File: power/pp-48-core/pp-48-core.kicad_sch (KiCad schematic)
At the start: 0 parts

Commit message: pp-48 chained plane: unit board 76 x 72 (9 mm left margin for chain IN J301 + holes, user; slots as rev1 at x 100 / 125; 17 mm input strip with XT60, unit hot-swap, chain OUT J302) and core board 56 x 72 (rev1 core minus the tile, 8 mm right margin for chain OUT J301 + holes, mux U6 by the header, XT30 at the bottom) placed as drafts by tools/place_unit.py / place_core.py (boardfit.py helpers); chain headers on B, pins at v 39..61 on every board; pinout swapped so IN pin 1 = 3V3 / P0 at the bottom on B (flat cable n -> 13 - n); DRC 0 errors besides unconnected, parity clean; not routed; handoff
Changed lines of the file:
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@@
+			)
+		)
+		(pin "UNIT4_SCL" bidirectional
+			(at 127 193.04 180)
+			(effects
+				(font
+					(size 1.27 1.27)
+				)
+				(justify left)
+			)
+		)
+		(pin "UNIT4_SDA" bidirectional
+			(at 127 195.58 180)
+			(effects
+				(font
+					(size 1.27 1.27)
+				)
+				(justify left)
+			)
+		)
+		(pin "UNIT3_SCL" bidirectional
+			(at 127 198.12 180)
+			(effects
+				(font
+					(size 1.27 1.27)
+				)
+				(justify left)
+			)
+		)
+		(pin "UNIT3_SDA" bidirectional
+			(at 127 200.66 180)
+			(effects
+				(font
+					(size 1.27 1.27)
+				)
+				(justify left)
+			)
+		)
+		(pin "UNIT2_SCL" bidirectional
+			(at 127 203.2 180)
+			(effects
+				(font
+					(size 1.27 1.27)
+				)
+				(justify left)
+			)
+		)
+		(pin "UNIT2_SDA" bidirectional
+			(at 127 205.74 180)
+			(effects
+				(font
+					(size 1.27 1.27)
+				)
+				(justify left)
+			)
+		)
+		(pin "UNIT1_SCL" bidirectional
+			(at 127 208.28 180)
+			(effects
+				(font
+					(size 1.27 1.27)
+				)
+				(justify left)
 			)
 		)
 		(pin "UNIT1_SDA" bidirectional
-			(at 127 193.04 180)
-			(effects
-				(font
-					(size 1.27 1.27)
-				)
-				(justify left)
-			)
-		)
-		(pin "UNIT1_SCL" bidirectional
-			(at 127 195.58 180)
-			(effects
-				(font
-					(size 1.27 1.27)
-				)
-				(justify left)
-			)
-		)
-		(pin "UNIT2_SDA" bidirectional
-			(at 127 198.12 180)
-			(effects
-				(font
-					(size 1.27 1.27)
-				)
-				(justify left)
-			)
-		)
-		(pin "UNIT2_SCL" bidirectional
-			(at 127 200.66 180)
-			(effects
-				(font
-					(size 1.27 1.27)
-				)
-				(justify left)
-			)
-		)
-		(pin "UNIT3_SDA" bidirectional
-			(at 127 203.2 180)
-			(effects
-				(font
-					(size 1.27 1.27)
-				)
-				(justify left)
-			)
-		)
-		(pin "UNIT3_SCL" bidirectional
-			(at 127 205.74 180)
-			(effects
-				(font
-					(size 1.27 1.27)
-				)
-				(justify left)
-			)
-		)
-		(pin "UNIT4_SDA" bidirectional
-			(at 127 208.28 180)
-			(effects
-				(font
-					(size 1.27 1.27)
-				)
-				(justify left)
-			)
-		)
-		(pin "UNIT4_SCL" bidirectional
 			(at 127 210.82 180)
 			(effects
@@
 		)
 	)
+	(label "UNIT4_SCL"
+		(at 119.38 193.04 180)
+		(effects
+			(font
+				(size 1.27 1.27)
+			)
+			(justify right bottom)
+		)
+	)
+	(wire
+		(pts
+			(xy 127 195.58) (xy 119.38 195.58)
+		)
+		(stroke
+			(width 0)
+			(type default)
+		)
+	)
+	(label "UNIT4_SDA"
+		(at 119.38 195.58 180)
+		(effects
+			(font
+				(size 1.27 1.27)
+			)
+			(justify right bottom)
+		)
+	)
+	(wire
+		(pts
+			(xy 127 198.12) (xy 119.38 198.12)
+		)
+		(stroke
+			(width 0)
+			(type default)
+		)
+	)
+	(label "UNIT3_SCL"
+		(at 119.38 198.12 180)
+		(effects
+			(font
+				(size 1.27 1.27)
+			)
+			(justify right bottom)
+		)
+	)
+	(wire
+		(pts
+			(xy 127 200.66) (xy 119.38 200.66)
+		)
+		(stroke
+			(width 0)
+			(type default)
+		)
+	)
+	(label "UNIT3_SDA"
+		(at 119.38 200.66 180)
+		(effects
+			(font
+				(size 1.27 1.27)
+			)
+			(justify right bottom)
+		)
+	)
+	(wire
+		(pts
+			(xy 127 203.2) (xy 119.38 203.2)
+		)
+		(stroke
+			(width 0)
+			(type default)
+		)
+	)
+	(label "UNIT2_SCL"
+		(at 119.38 203.2 180)
+		(effects
+			(font
+				(size 1.27 1.27)
+			)
+			(justify right bottom)
+		)
+	)
+	(wire
+		(pts
+			(xy 127 205.74) (xy 119.38 205.74)
+		)
+		(stroke
+			(width 0)
+			(type default)
+		)
+	)
+	(label "UNIT2_SDA"
+		(at 119.38 205.74 180)
+		(effects
+			(font
+				(size 1.27 1.27)
+			)
+			(justify right bottom)
+		)
+	)
+	(wire
+		(pts
+			(xy 127 208.28) (xy 119.38 208.28)
+		)
+		(stroke
+			(width 0)
+			(type default)
+		)
+	)
+	(label "UNIT1_SCL"
+		(at 119.38 208.28 180)
+		(effects
+			(font
+				(size 1.27 1.27)
+			)
+			(justify right bottom)
+		)
+	)
+	(wire
+		(pts
+			(xy 127 210.82) (xy 119.38 210.82)
+		)
+		(stroke
+			(width 0)
+			(type default)
+		)
+	)
 	(label "UNIT1_SDA"
-		(at 119.38 193.04 180)
-		(effects
-			(font
-				(size 1.27 1.27)
-			)
-			(justify right bottom)
-		)
-	)
-	(wire
-		(pts
-			(xy 127 195.58) (xy 119.38 195.58)
-		)
-		(stroke
-			(width 0)
-			(type default)
-		)
-	)
-	(label "UNIT1_SCL"
-		(at 119.38 195.58 180)
-		(effects
-			(font
-				(size 1.27 1.27)
-			)
-			(justify right bottom)
-		)
-	)
-	(wire
-		(pts
-			(xy 127 198.12) (xy 119.38 198.12)
-		)
-		(stroke
-			(width 0)
-			(type default)
-		)
-	)
-	(label "UNIT2_SDA"
-		(at 119.38 198.12 180)
-		(effects
-			(font
-				(size 1.27 1.27)
-			)
-			(justify right bottom)
-		)
-	)
-	(wire
-		(pts
-			(xy 127 200.66) (xy 119.38 200.66)
-		)
-		(stroke
-			(width 0)
-			(type default)
-		)
-	)
-	(label "UNIT2_SCL"
-		(at 119.38 200.66 180)
-		(effects
-			(font
-				(size 1.27 1.27)
-			)
-			(justify right bottom)
-		)
-	)
-	(wire
-		(pts
-			(xy 127 203.2) (xy 119.38 203.2)
-		)
-		(stroke
-			(width 0)
-			(type default)
-		)
-	)
-	(label "UNIT3_SDA"
-		(at 119.38 203.2 180)
-		(effects
-			(font
-				(size 1.27 1.27)
-			)
-			(justify right bottom)
-		)
-	)
-	(wire
-		(pts
-			(xy 127 205.74) (xy 119.38 205.74)
-		)
-		(stroke
-			(width 0)
-			(type default)
-		)
-	)
-	(label "UNIT3_SCL"
-		(at 119.38 205.74 180)
-		(effects
-			(font
-				(size 1.27 1.27)
-			)
-			(justify right bottom)
-		)
-	)
-	(wire
-		(pts
-			(xy 127 208.28) (xy 119.38 208.28)
-		)
-		(stroke
-			(width 0)
-			(type default)
-		)
-	)
-	(label "UNIT4_SDA"
-		(at 119.38 208.28 180)
-		(effects
-			(font
-				(size 1.27 1.27)
-			)
-			(justify right bottom)
-		)
-	)
-	(wire
-		(pts
-			(xy 127 210.82) (xy 119.38 210.82)
-		)
-		(stroke
-			(width 0)
-			(type default)
-		)
-	)
-	(label "UNIT4_SCL"
 		(at 119.38 210.82 180)
 		(effects

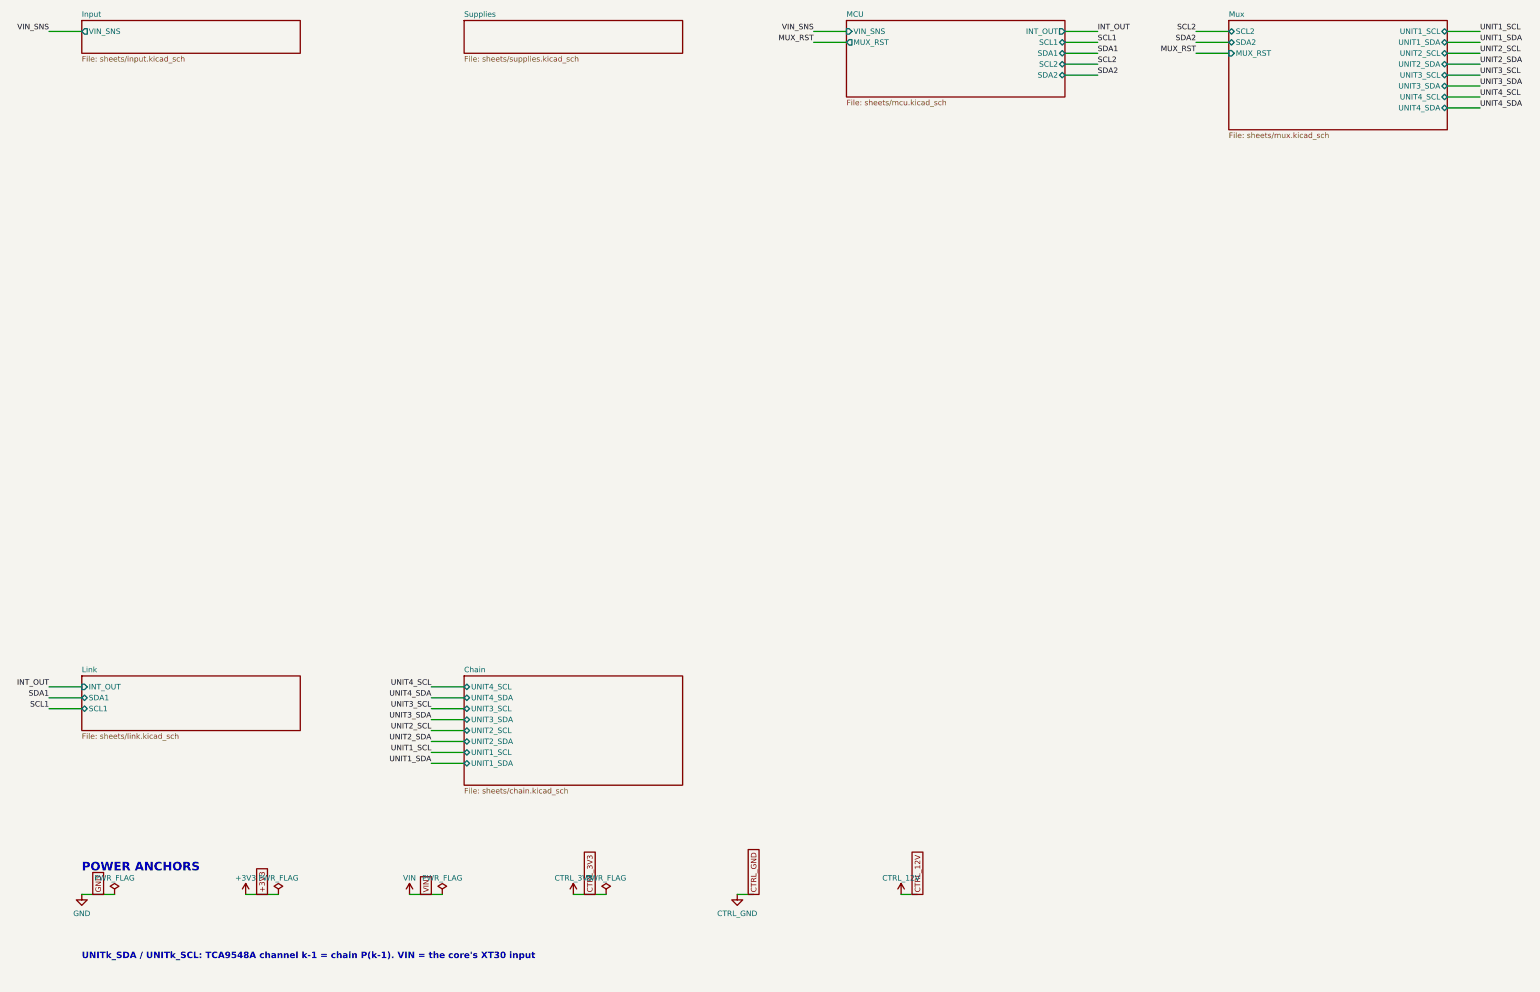
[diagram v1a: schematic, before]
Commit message: pp-48 plane boards: press deadline line (docs/press-deadline-line.md decided: option B + A) on a 14-pin chain (S14B-PH-K-S C157938; 13 PRESS_EN, 14 EXP_RSTN, cable n -> 15 - n, pins v 35..61); unit Q10 / R31 switch the photoMOS LED returns (PRESS_RTN), core U301 74LVC1G123 deadline (pp:74LVC1G123 single-unit copy) on PC6 PRESS_TRIG, PC7 EXP_RSTN to the units' /RESET; ERC 0 both; boards rebuilt and placed, unit 78.5 x 72 with the strip power path re-placed top-down; unit routing tools (route_unit.py hand copper + In2 band / +3V3 trunk, unitsplit.py, route_unit.sh flow): DRC 0 errors, ~10 unconnected at expander U5; core placed, not routed; pmmount.py restored from granite_controller; ADR 0005 decision 4; handoff
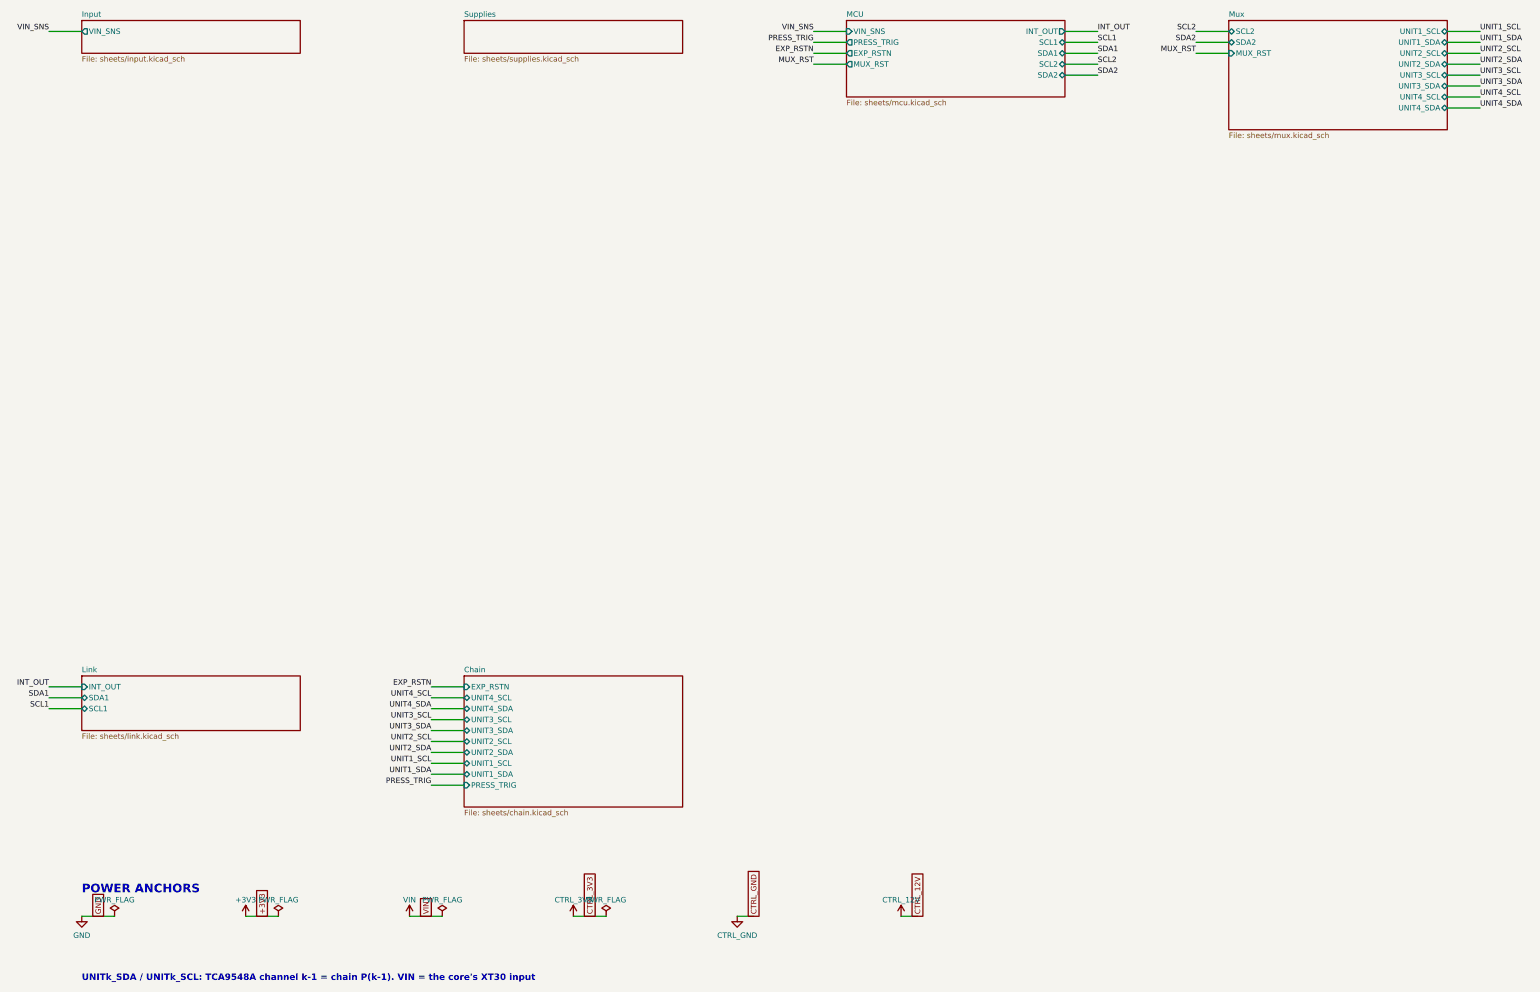
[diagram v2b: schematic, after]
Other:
- sheet Chain ports: added EXP_RSTN, PRESS_TRIG; removed none
- sheet MCU ports: added EXP_RSTN, PRESS_TRIG; removed none

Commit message: pp-48 core Supplies: LM5017 Fly-Buck replaces the interim 12 V module (ADR 0003 decision 14): L2 SRF0703-470M on the new footprint pp48:L_Bourns_SRF0703, secondary on the CTRL_GND island, PWR_FLAGs on CTRL_12V / CTRL_GND; ERC 0; handoff updated
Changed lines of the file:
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@@
 	(wire
 		(pts
-			(xy 190.5 246.38) (xy 194.31 246.38)
+			(xy 190.5 246.38) (xy 198.12 246.38)
 		)
 		(stroke
@@
 				(font
 					(size 1.27 1.27)
+				)
+			)
+		)
+	)
+	(symbol
+		(lib_id "power:PWR_FLAG")
+		(at 198.12 246.38 0)
+		(unit 1)
+		(body_style 1)
+		(exclude_from_sim no)
+		(in_bom no)
+		(on_board no)
+		(in_pos_files yes)
+		(dnp no)
+		(property "Reference" "#FLG9010"
+			(at 198.12 246.38 0)
+			(hide yes)
+			(show_name no)
+			(do_not_autoplace no)
+			(effects
+				(font
+					(size 1.27 1.27)
+				)
+			)
+		)
+		(property "Value" "PWR_FLAG"
+			(at 198.12 242.57 0)
+			(show_name no)
+			(do_not_autoplace no)
+			(effects
+				(font
+					(size 1.27 1.27)
+				)
+			)
+		)
+		(property "Footprint" ""
+			(at 198.12 246.38 0)
+			(hide yes)
+			(show_name no)
+			(do_not_autoplace no)
+			(effects
+				(font
+					(size 1.27 1.27)
+				)
+				(justify left)
+			)
+		)
+		(property "Datasheet" ""
+			(at 198.12 246.38 0)
+			(hide yes)
+			(show_name no)
+			(do_not_autoplace no)
+			(effects
+				(font
+					(size 1.27 1.27)
+				)
+				(justify left)
+			)
+		)
+		(property "Description" ""
+			(at 198.12 246.38 0)
+			(hide yes)
+			(show_name no)
+			(do_not_autoplace no)
+			(effects
+				(font
+					(size 1.27 1.27)
+				)
+				(justify left)
+			)
+		)
+		(pin "1"
+		)
+		(instances
+			(project "pp-48-core"
+				(path "/2947a401-cd9a-5ee7-8a9d-b67547832ff9"
+					(reference "#FLG9010")
+					(unit 1)
 				)
 			)
@@
 		(in_pos_files yes)
 		(dnp no)
-		(property "Reference" "#PWR9010"
+		(property "Reference" "#PWR9011"
 			(at 228.6 246.38 0)
 			(hide yes)
@@
 			(project "pp-48-core"
 				(path "/2947a401-cd9a-5ee7-8a9d-b67547832ff9"
-					(reference "#PWR9010")
+					(reference "#PWR9011")
 					(unit 1)
 				)
@@
 	(wire
 		(pts
-			(xy 228.6 246.38) (xy 232.41 246.38)
+			(xy 228.6 246.38) (xy 236.22 246.38)
 		)
 		(stroke
@@
 				)
 			)
+		)
+	)
+	(symbol
+		(lib_id "power:PWR_FLAG")
+		(at 236.22 246.38 0)
+		(unit 1)
+		(body_style 1)
+		(exclude_from_sim no)
+		(in_bom no)
+		(on_board no)
+		(in_pos_files yes)
+		(dnp no)
+		(property "Reference" "#FLG9012"
+			(at 236.22 246.38 0)
+			(hide yes)
+			(show_name no)
+			(do_not_autoplace no)
+			(effects
+				(font
+					(size 1.27 1.27)
+				)
+			)
+		)
+		(property "Value" "PWR_FLAG"
+			(at 236.22 242.57 0)
+			(show_name no)
+			(do_not_autoplace no)
+			(effects
+				(font
+					(size 1.27 1.27)
+				)
+			)
+		)
+		(property "Footprint" ""
+			(at 236.22 246.38 0)
+			(hide yes)
+			(show_name no)
+			(do_not_autoplace no)
+			(effects
+				(font
+					(size 1.27 1.27)
+				)
+				(justify left)
+			)
+		)
+		(property "Datasheet" ""
+			(at 236.22 246.38 0)
+			(hide yes)
+			(show_name no)
+			(do_not_autoplace no)
+			(effects
+				(font
+					(size 1.27 1.27)
+				)
+				(justify left)
+			)
+		)
+		(property "Description" ""
+			(at 236.22 246.38 0)
+			(hide yes)
+			(show_name no)
+			(do_not_autoplace no)
+			(effects
+				(font
+					(size 1.27 1.27)
+				)
+				(justify left)
+			)
+		)
+		(pin "1"
+		)
+		(instances
+			(project "pp-48-core"
+				(path "/2947a401-cd9a-5ee7-8a9d-b67547832ff9"
+					(reference "#FLG9012")
+					(unit 1)
+				)
+			)
